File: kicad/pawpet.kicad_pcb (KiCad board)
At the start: 2 copper layers, 51.8 x 51.8 mm, 41 parts, among them J1 USB4105-GF-A, J2 Conn_ARM_JTAG_SWD_10, J3 MOLEX, Q1 DMG2301L, U1 ATSAMD21G18A-A, U3 MX25R1635FM1IL0, Y1 32,768

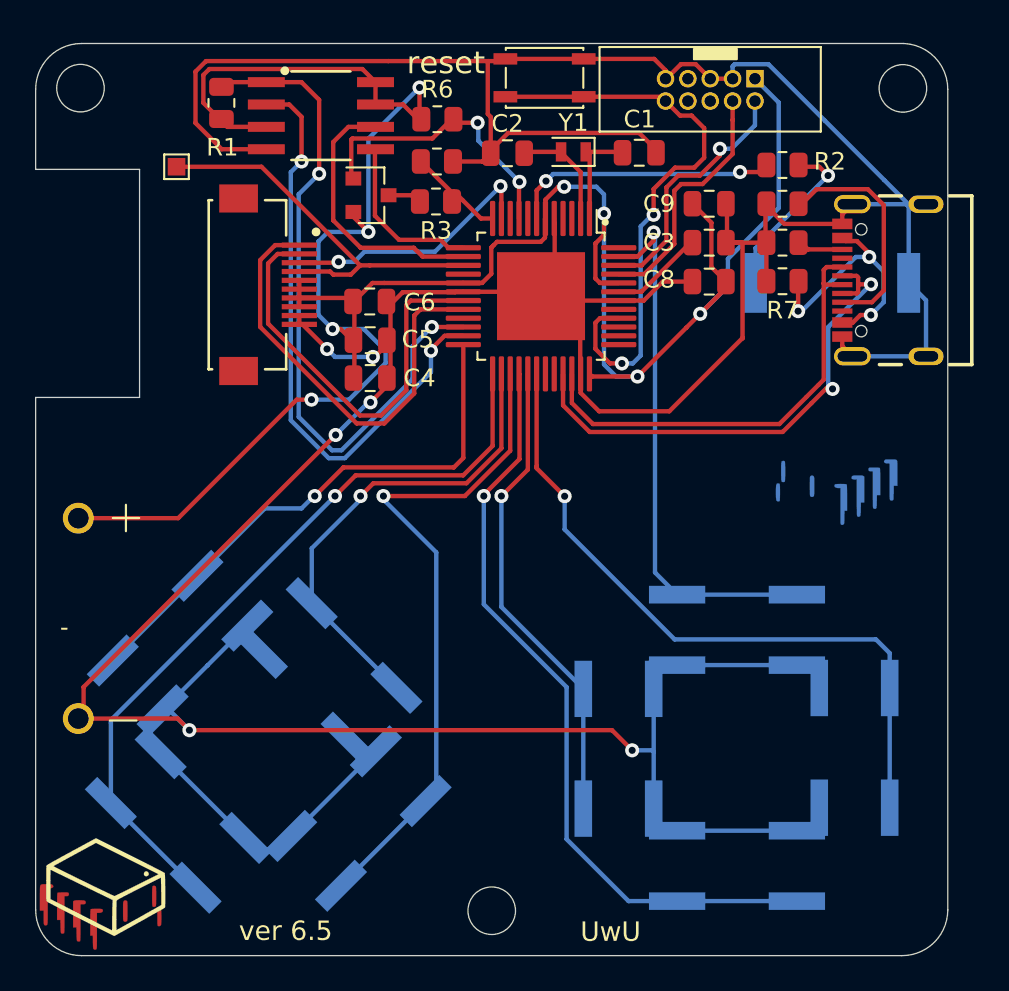
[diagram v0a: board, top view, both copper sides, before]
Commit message: updated to use latest adafruit samd base and gclk output to display vcom
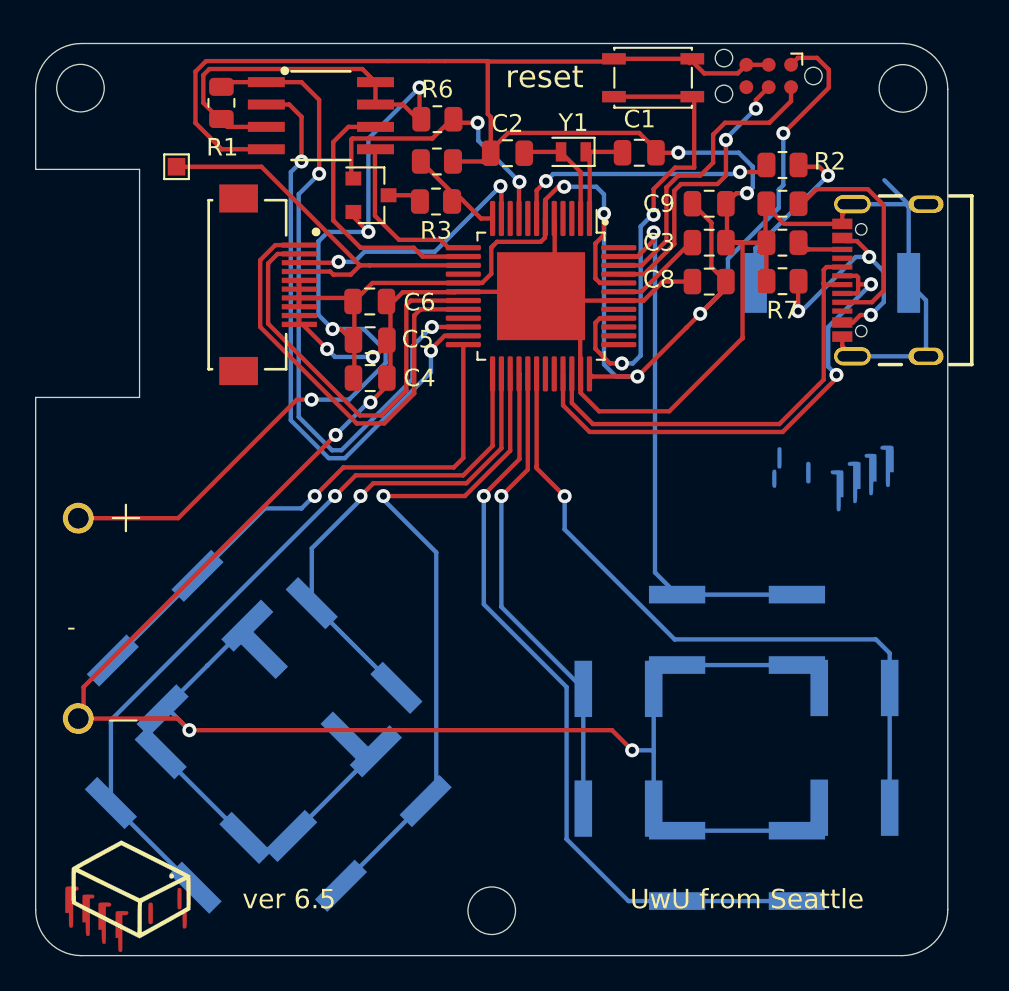
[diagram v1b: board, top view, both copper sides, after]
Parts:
- J2: footprint pawpet:ARM_JTAG -> Connector:Tag-Connect_TC2030-IDC-NL_2x03_P1.27mm_Vertical
- R2: value 1k -> 470
- moved SW_reset1 6.17 mm to (166.4, 65.9)
- moved Ref** 1.45 mm to (135.4, 112.8)
- moved Ref** 0.80 mm to (177.6, 87.8)
- moved J2 0.80 mm to (172.9, 65.8), turned to 180 degrees
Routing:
- net /reset: track 33.1 -> 26.9 mm
- net +3V3: track 144.1 -> 147.8 mm, vias 8 -> 9
- net /SWDIO: track 14.4 -> 17.1 mm, vias 1 -> 0
- net GND: track 283.0 -> 280.8 mm, vias 6 -> 8
- net /SWCLK: track 14.1 -> 16.2 mm, vias 0 -> 2
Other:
- board text added: "UwU from Seattle"
- board text removed: "UwU"

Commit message: update to latest schematic, pcb, and stl files
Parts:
- J3: footprint pawpet:Molex-52892-1033-Manufacturer_Recommended_handsolder -> molex:Molex-52892-1033-Manufacturer_Recommended
- U1: footprint pawpet:TQFP-48-1EP_7x7mm_P0.5mm_EP5x5mm_handsolder -> Package_QFP:TQFP-48-1EP_7x7mm_P0.5mm_EP5x5mm
- U3: footprint pawpet:Macronix-SOP-8-150MIL-0-0-MFG_handsolder -> Package_SO:SOIC-8_5.23x5.23mm_P1.27mm
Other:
- board text added: "ver 6.6"
- board text removed: "ver 6.5"
